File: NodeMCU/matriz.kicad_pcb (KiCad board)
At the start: 2 copper layers, 17 parts, among them J1 Conn_01x05, Q1 Q_NPN_BCE, Q2 Q_NPN_BCE, Q3 Q_NPN_BCE, SW1 SW_Push_Open, SW2 SW_Push, U3 NodeMCU1.0(ESP-12E)

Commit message: avances master
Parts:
- added w2.1: , Wire_Pads:SolderWirePad_single_0-8mmDrill, F.Cu at (97.8, 81.3)
- added w2.2: , Wire_Pads:SolderWirePad_single_0-8mmDrill, F.Cu at (97.8, 86.4)
- moved Q2 17.3 mm to (137.2, 95.2)
- moved R3 1.91 mm to (101.6, 86.4)
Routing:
- net /CLK: track 14.3 -> 96.7 mm
- net /LD: track 74.0 -> 47.6 mm
- net Net-(Q2-Pad1): track 57.8 -> 44.7 mm
- net /V+: track 252.7 -> 260.8 mm
- net Net-(R1-Pad2): track 27.7 -> 31.0 mm
- net Net-(R3-Pad2): track 6.07 -> 7.98 mm

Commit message: Cosas del dia 30 en barcara
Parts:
- removed w2.1, w2.2: , Wire_Pads:SolderWirePad_single_0-8mmDrill
- Q1, Q2, Q3: value Q_NPN_BCE -> Q_NPN_CBE
- U3: footprint NodeMCU:NodeMCU1.0(12-E) -> ESP8266:NodeMCU1.0(12-E)
- moved R2 69.8 mm to (188.0, 120.0), turned to 90 degrees
- moved R6 65.1 mm to (188.0, 96.5), turned to 270 degrees
- moved R4 52.5 mm to (172.1, 108.6)
- moved J1 49.5 mm to (189.9, 70.5)
- moved JP3 46.0 mm to (125.7, 71.8)
- moved JP4 44.9 mm to (135.3, 71.8)
- moved JP2 44.3 mm to (116.2, 71.8)
- moved SW2 44.3 mm to (144.8, 71.8)
- moved JP1 43.7 mm to (106.0, 71.8)
- moved R3 42.6 mm to (141.6, 101.0)
- moved SW1 42.3 mm to (94.6, 71.8)
- moved Q3 34.1 mm to (176.5, 86.4), turned to 90 degrees
- moved R1 31.8 mm to (127.6, 102.9)
- moved R5 31.0 mm to (156.2, 90.2)
- moved U3 29.9 mm to (106.0, 108.0)
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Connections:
- Q1 pad 1: Net-(Q1-Pad1) -> /CLK
- Q1 pad 2: /V+ -> Net-(Q1-Pad2)
- Q1 pad 3: /CLK -> GNDPWR
- Q2 pad 1: Net-(Q2-Pad1) -> /LD
- Q2 pad 2: /V+ -> Net-(Q2-Pad2)
- Q2 pad 3: /LD -> GNDPWR
- Q3 pad 1: Net-(Q3-Pad1) -> /DOUT
- Q3 pad 2: /V+ -> Net-(Q3-Pad2)
- Q3 pad 3: /DOUT -> GNDPWR
- R1 pad 1: Net-(Q1-Pad1) -> Net-(Q1-Pad2)
- R2 pad 1: GNDPWR -> /CLK
- R2 pad 2: /CLK -> /V+
- R3 pad 1: Net-(Q2-Pad1) -> Net-(Q2-Pad2)
- R4 pad 1: GNDPWR -> /LD
- R4 pad 2: /LD -> /V+
- R5 pad 1: Net-(Q3-Pad1) -> Net-(Q3-Pad2)
- R6 pad 1: GNDPWR -> /DOUT
- R6 pad 2: /DOUT -> /V+
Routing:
- net GNDPWR: track 154.6 -> 334.0 mm
- net /LD: track 47.6 -> 93.6 mm
- net Net-(Q2-Pad1): track 44.7 -> 0.00 mm
- net /V+: track 260.8 -> 220.0 mm
- net /CLK: track 96.7 -> 131.8 mm
- net Net-(R1-Pad2): track 31.0 -> 7.62 mm
- net Net-(Q3-Pad2): track 0.00 -> 19.9 mm
- net Net-(Q3-Pad1): track 15.7 -> 0.00 mm
- net /DOUT: track 57.3 -> 42.7 mm
- net Net-(R3-Pad2): track 7.98 -> 21.9 mm
- net Net-(Q2-Pad2): track 0.00 -> 11.6 mm
- net Net-(SW2-Pad2): track 42.0 -> 53.0 mm
- net Net-(Q1-Pad2): track 0.00 -> 10.4 mm
- net Net-(Q1-Pad1): track 10.3 -> 0.00 mm
- net Net-(JP2-Pad1): track 56.6 -> 48.0 mm
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
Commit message: Pistas todas de 1mm, limite y unidades mecanicas
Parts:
- added REF**: 1pin, Connectors:1pin, F.Cu at (153.0, 131.0)
- added REF**: 1pin, Connectors:1pin, F.Cu at (153.0, 68.0)
- added REF**: 1pin, Connectors:1pin, F.Cu at (88.0, 131.0)
- added REF**: 1pin, Connectors:1pin, F.Cu at (89.0, 68.0)
- J1: footprint Pin_Headers:Pin_Header_Angled_1x05_Pitch2.54mm -> Pin_Headers:Pin_Header_Straight_1x05_Pitch2.54mm
- moved R2 51.2 mm to (137.0, 115.0), turned to 0 degrees
- moved J1 47.1 mm to (143.0, 75.0)
- moved R6 44.5 mm to (145.0, 85.0)
- moved Q3 42.7 mm to (134.0, 83.0)
- moved R4 35.1 mm to (137.0, 109.0)
- moved Q2 16.0 mm to (139.0, 101.0)
- moved R5 15.5 mm to (141.0, 93.0)
- moved R3 11.8 mm to (130.0, 103.0)
- moved SW2 9.78 mm to (135.0, 72.0)
- moved JP4 8.26 mm to (127.0, 72.0)
- moved JP3 6.73 mm to (119.0, 72.0)
- moved JP2 5.21 mm to (111.0, 72.0)
- moved Q1 4.36 mm to (129.0, 112.0)
- moved JP1 4.00 mm to (102.0, 71.8)
- moved R1 3.64 mm to (124.0, 103.0)
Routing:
- net GNDPWR: track 334.0 -> 263.4 mm
- net /V+: track 220.0 -> 164.5 mm
- net /CLK: track 131.8 -> 83.0 mm
- net /LD: track 93.6 -> 72.7 mm
- net Net-(R5-Pad2): track 28.6 -> 15.0 mm
- net Net-(SW2-Pad2): track 53.0 -> 40.4 mm
- net /DOUT: track 42.7 -> 30.5 mm
- net Net-(JP4-Pad1): track 53.1 -> 41.3 mm
- net Net-(R3-Pad2): track 21.9 -> 11.1 mm
- net Net-(JP3-Pad1): track 50.6 -> 43.6 mm
- net Net-(JP1-Pad2): track 35.5 -> 30.2 mm
- net Net-(Q3-Pad2): track 19.9 -> 15.5 mm
- net Net-(R1-Pad2): track 7.62 -> 4.04 mm
- net Net-(Q2-Pad2): track 11.6 -> 8.41 mm
- net Net-(JP2-Pad1): track 48.0 -> 46.2 mm
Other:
- board outline added: 75 x 73 mm
- net class Default: trace_width 0.6 -> 1

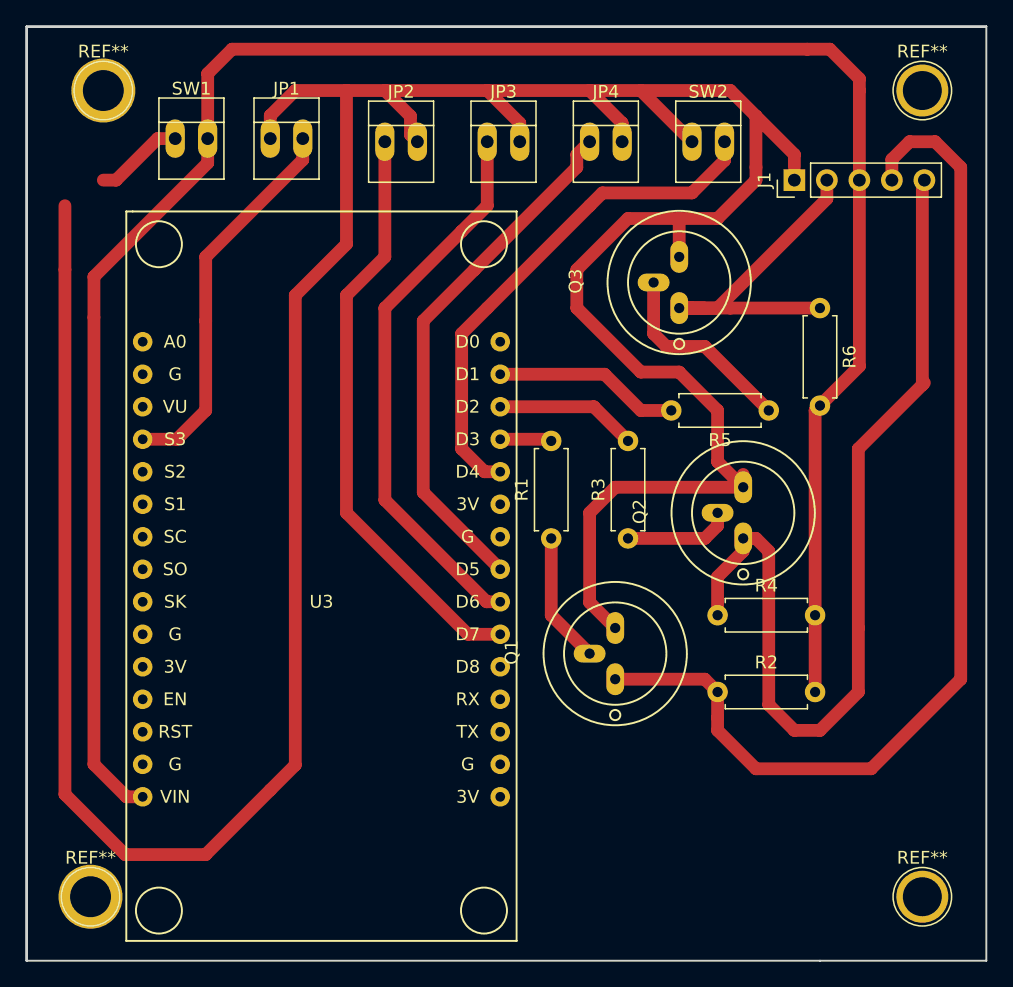
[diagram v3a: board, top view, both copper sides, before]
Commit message: Saco un jumprs y reacomodo
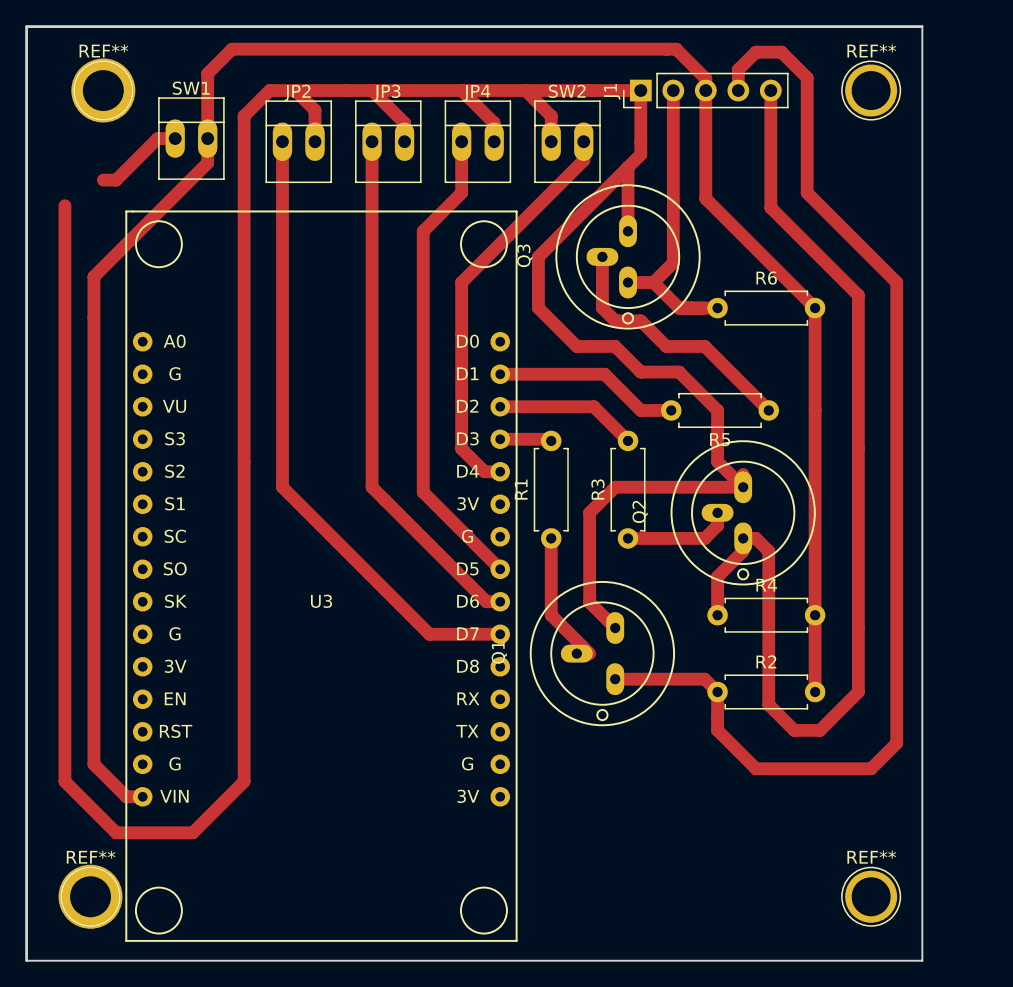
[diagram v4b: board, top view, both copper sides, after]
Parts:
- removed JP1: Jp_open_small, Connectors:PINHEAD1-2
- moved J1 13.9 mm to (131.0, 68.0)
- moved SW2 11.0 mm to (124.0, 72.0)
- moved JP4 10.0 mm to (117.0, 72.0)
- moved JP3 9.00 mm to (110.0, 72.0)
- moved JP2 8.00 mm to (103.0, 72.0)
- moved R6 8.00 mm to (137.0, 85.0), turned to 0 degrees
- moved Q3 4.47 mm to (130.0, 81.0)
- moved REF** 4.00 mm to (149.0, 131.0)
- moved REF** 4.00 mm to (149.0, 68.0)
- moved Q1 1.00 mm to (128.0, 112.0)
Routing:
- net Net-(U3-Pad4): track 30.2 -> 0.00 mm
- net GNDPWR: track 263.4 -> 238.8 mm
- net /V+: track 164.5 -> 154.6 mm
- net Net-(SW2-Pad2): track 40.4 -> 31.7 mm
- net /CLK: track 83.0 -> 90.8 mm
- net /LD: track 72.7 -> 80.1 mm
- net Net-(Q3-Pad2): track 15.5 -> 20.3 mm
- net Net-(JP4-Pad1): track 41.3 -> 37.1 mm
- net /DOUT: track 30.5 -> 26.5 mm
- net Net-(JP3-Pad1): track 43.6 -> 40.7 mm
- net Net-(JP2-Pad1): track 46.2 -> 48.8 mm
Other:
- board size 75 x 73 mm -> 70 x 73 mm

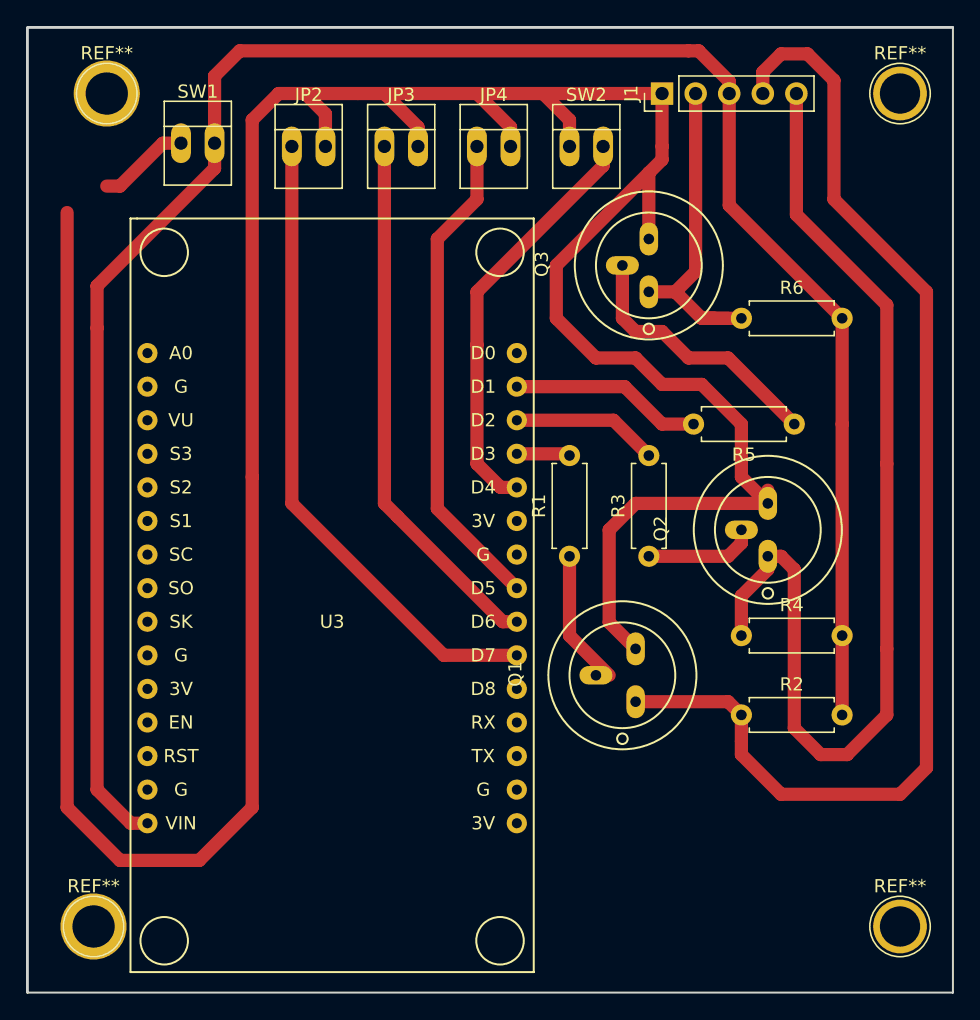
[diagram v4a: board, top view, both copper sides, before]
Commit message: Pongo las pistas en para que sea lo de atras (en verde) y minimiso espacio
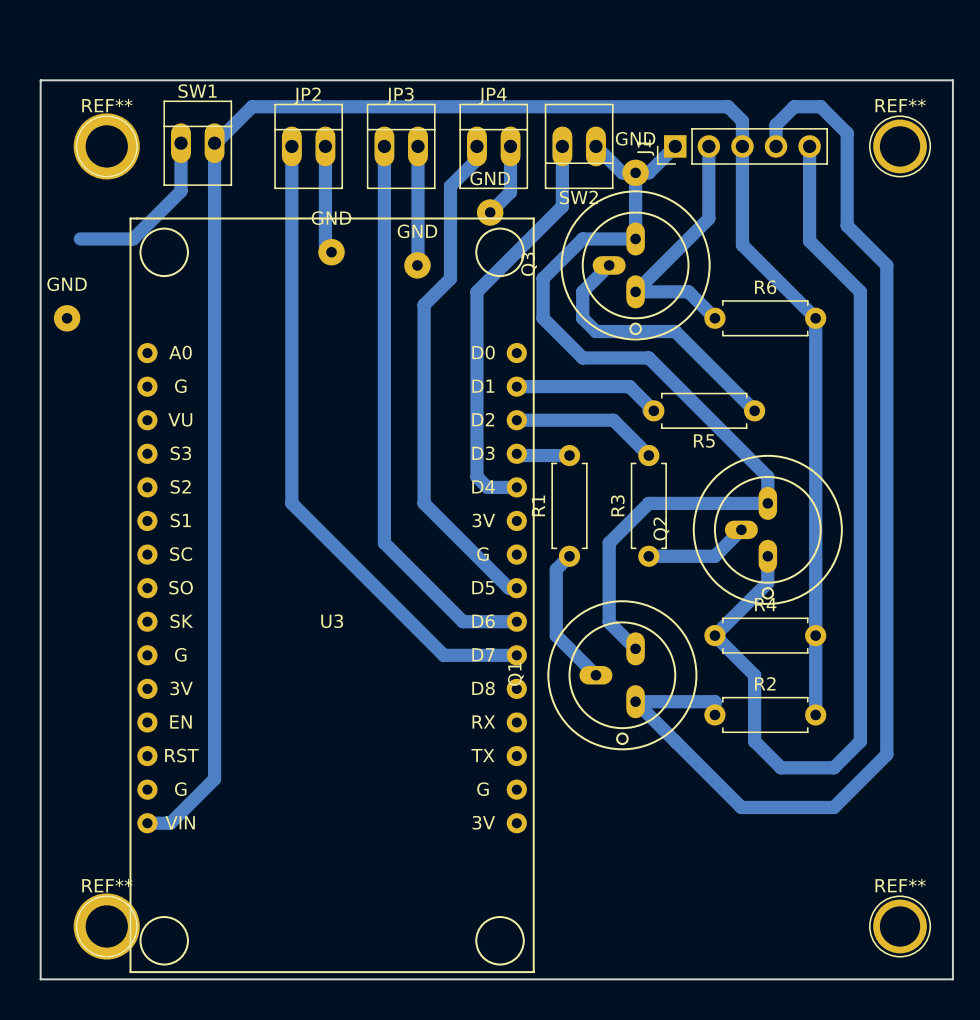
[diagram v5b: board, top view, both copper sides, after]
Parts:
- added GND: , Wire_Pads:SolderWirePad_single_0-8mmDrill, F.Cu at (106.0, 80.0)
- added GND: , Wire_Pads:SolderWirePad_single_0-8mmDrill, F.Cu at (118.0, 77.0)
- added GND: , Wire_Pads:SolderWirePad_single_0-8mmDrill, F.Cu at (129.0, 74.0)
- added GND: , Wire_Pads:SolderWirePad_single_0-8mmDrill, F.Cu at (112.5, 81.0)
- added GND: , Wire_Pads:SolderWirePad_single_0-8mmDrill, F.Cu at (86.0, 85.0)
- moved J1 4.12 mm to (132.0, 72.0)
- moved REF** 4.00 mm to (149.0, 72.0)
- moved REF** 4.00 mm to (89.0, 72.0)
- moved R5 3.16 mm to (138.0, 92.0)
- moved R2 2.00 mm to (135.0, 115.0)
- moved R4 2.00 mm to (135.0, 109.0)
- moved R6 2.00 mm to (135.0, 85.0)
- moved SW2 2.00 mm to (126.0, 72.0), turned to 180 degrees
- moved Q3 1.00 mm to (129.0, 81.0)
- moved REF** 1.00 mm to (89.0, 131.0)
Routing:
- net GNDPWR: track 238.8 -> 92.8 mm
- net /V+: track 154.6 -> 143.3 mm
- net /LD: track 80.1 -> 73.1 mm
- net /DOUT: track 26.5 -> 20.1 mm
- net +5V: track 6.96 -> 12.7 mm
- net Net-(R5-Pad2): track 15.0 -> 11.5 mm
- net /CLK: track 90.8 -> 87.6 mm
- net Net-(JP3-Pad1): track 40.7 -> 42.5 mm
- net Net-(JP4-Pad1): track 37.1 -> 38.3 mm
- net Net-(SW2-Pad2): track 31.7 -> 31.0 mm
- net Net-(Q2-Pad2): track 8.41 -> 7.83 mm
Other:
- board size 70 x 73 mm -> 69 x 68 mm

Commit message: Avances entre todos
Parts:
- R1, R3, R5: value 50KOhm -> 500Ohm
- R2, R6: value 0.7KOhm -> 1000KOhm
- R4: value 0.7KOhm -> 1000Ohm
- moved GND 0.50 mm to (129.0, 74.5)
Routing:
- net GNDPWR: track 92.8 -> 93.5 mm
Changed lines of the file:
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@@
     (links 32)
     (no_connects 3)
-    (area 82.924999 62.924999 165.85 143.700001)
+    (area 83.924999 66.88 164.85 141.700001)
     (thickness 1.6)
     (drawings 6)
-    (tracks 99)
+    (tracks 98)
     (zones 0)
     (modules 25)
@@
     (mod_text_size 1 1)
     (mod_text_width 0.15)
-    (pad_size 1.99898 1.99898)
-    (pad_drill 0.8001)
+    (pad_size 4.5 4.5)
+    (pad_drill 4)
     (pad_to_mask_clearance 0.2)
     (aux_axis_origin 0 0)
     (visible_elements 7FFFFFFF)
     (pcbplotparams
-      (layerselection 0x00030_80000001)
+      (layerselection 0x00000_80000000)
       (usegerberextensions false)
       (excludeedgelayer true)
-      (linewidth 0.100000)
+      (linewidth 1.000000)
       (plotframeref false)
       (viasonmask false)
@@
       (padsonsilk false)
       (subtractmaskfromsilk false)
-      (outputformat 1)
+      (outputformat 4)
       (mirror false)
-      (drillshape 1)
+      (drillshape 0)
       (scaleselection 1)
-      (outputdirectory ""))
+      (outputdirectory C:/Users/nahuel/git/conexiones/))
   )
   (net 0 "")
@@
       (effects (font (size 1 1) (thickness 0.15)))
     )
-    (fp_text value 50KOhm (at 3.81 2.31 90) (layer F.Fab)
+    (fp_text value 500Ohm (at 3.81 2.31 90) (layer F.Fab)
       (effects (font (size 1 1) (thickness 0.15)))
     )
@@
       (effects (font (size 1 1) (thickness 0.15)))
     )
-    (fp_text value 0.7KOhm (at 3.81 2.31) (layer F.Fab)
+    (fp_text value 1000KOhm (at 3.81 2.31) (layer F.Fab)
       (effects (font (size 1 1) (thickness 0.15)))
     )
@@
       (effects (font (size 1 1) (thickness 0.15)))
     )
-    (fp_text value 50KOhm (at 3.81 2.31 90) (layer F.Fab)
+    (fp_text value 500Ohm (at 3.81 2.31 90) (layer F.Fab)
       (effects (font (size 1 1) (thickness 0.15)))
     )
@@
       (effects (font (size 1 1) (thickness 0.15)))
     )
-    (fp_text value 0.7KOhm (at 3.81 2.31) (layer F.Fab)
+    (fp_text value 1000Ohm (at 3.81 2.31) (layer F.Fab)
       (effects (font (size 1 1) (thickness 0.15)))
     )
@@
       (effects (font (size 1 1) (thickness 0.15)))
     )
-    (fp_text value 50KOhm (at 3.81 2.31 180) (layer F.Fab)
+    (fp_text value 500Ohm (at 3.81 2.31 180) (layer F.Fab)
       (effects (font (size 1 1) (thickness 0.15)))
     )
@@
       (effects (font (size 1 1) (thickness 0.15)))
     )
-    (fp_text value 0.7KOhm (at 3.81 2.31) (layer F.Fab)
+    (fp_text value 1000KOhm (at 3.81 2.31) (layer F.Fab)
       (effects (font (size 1 1) (thickness 0.15)))
     )
@@
     (fp_circle (center 0 0) (end 2.6 0) (layer F.CrtYd) (width 0.05))
     (fp_circle (center 0 0) (end 0 -2.286) (layer F.SilkS) (width 0.12))
-    (pad 1 thru_hole circle (at 0 0) (size 4.064 4.064) (drill 3.048) (layers *.Cu *.Mask))
+    (pad 1 thru_hole circle (at 0 0) (size 4.5 4.5) (drill 4) (layers *.Cu *.Mask))
   )
   (module Connectors:1pin (layer F.Cu)
@@
     (fp_circle (center 0 0) (end 2.6 0) (layer F.CrtYd) (width 0.05))
     (fp_circle (center 0 0) (end 0 -2.286) (layer F.SilkS) (width 0.12))
-    (pad 1 thru_hole circle (at 0 0) (size 4.064 4.064) (drill 3.048) (layers *.Cu *.Mask))
+    (pad 1 thru_hole circle (at 0 0) (size 4.5 4.5) (drill 4) (layers *.Cu *.Mask))
   )
   (module Connectors:1pin (layer F.Cu)
@@
     (fp_circle (center 0 0) (end 2.6 0) (layer F.CrtYd) (width 0.05))
     (fp_circle (center 0 0) (end 0 -2.286) (layer F.SilkS) (width 0.12))
-    (pad 1 thru_hole circle (at 0 0) (size 5 5) (drill 3.2) (layers *.Cu *.Mask))
+    (pad 1 thru_hole circle (at 0 0) (size 4.5 4.5) (drill 4) (layers *.Cu *.Mask))
   )
   (module Connectors:1pin (layer F.Cu)
@@
     (fp_circle (center 0 0) (end 2.6 0) (layer F.CrtYd) (width 0.05))
     (fp_circle (center 0 0) (end 0 -2.286) (layer F.SilkS) (width 0.12))
-    (pad 1 thru_hole circle (at 0 0) (size 5 5) (drill 3.2) (layers *.Cu *.Mask))
+    (pad 1 thru_hole circle (at 0 0) (size 4.5 4.5) (drill 4) (layers *.Cu *.Mask))
   )
   (module Wire_Pads:SolderWirePad_single_0-8mmDrill (layer F.Cu)
@@
   )
   (module Wire_Pads:SolderWirePad_single_0-8mmDrill (layer F.Cu)
-    (at 129 74)
+    (at 129 74.5)
     (fp_text reference GND (at 0 -2.54) (layer F.SilkS)
       (effects (font (size 1 1) (thickness 0.15)))
@@
   (gr_line (start 153 67) (end 153 135) (angle 90) (layer Edge.Cuts) (width 0.15))
   (gr_line (start 84 67) (end 153 67) (angle 90) (layer Edge.Cuts) (width 0.15))
+  (segment (start 105.54 72) (end 105.54 79.54) (width 1) (layer B.Cu) (net 1))
+  (segment (start 105.54 79.54) (end 106 80) (width 1) (layer B.Cu) (net 1))
+  (segment (start 129 79) (end 124.5 79) (width 1) (layer B.Cu) (net 1))
+  (segment (start 139 96.5) (end 139 99) (width 1) (layer B.Cu) (net 1))
+  (segment (start 130.5 88) (end 139 96.5) (width 1) (layer B.Cu) (net 1))
+  (segment (start 125 88) (end 130.5 88) (width 1) (layer B.Cu) (net 1))
+  (segment (start 123 86) (end 125 88) (width 1) (layer B.Cu) (net 1))
+  (segment (start 123 80.5) (end 123 86) (width 1) (layer B.Cu) (net 1))
+  (segment (start 124.5 79) (end 123 80.5) (width 1) (layer B.Cu) (net 1))
+  (segment (start 129 74.5) (end 129 79) (width 1) (layer B.Cu) (net 1))
   (segment (start 119.54 72) (end 119.54 75.46) (width 1) (layer B.Cu) (net 1))
   (segment (start 119.54 75.46) (end 118 77) (width 1) (layer B.Cu) (net 1))
   (segment (start 139 99) (end 130 99) (width 1) (layer B.Cu) (net 1))
+  (segment (start 130 99) (end 127 102) (width 1) (layer B.Cu) (net 1))
+  (segment (start 127 102) (end 127 108) (width 1) (layer B.Cu) (net 1))
   (segment (start 127 108) (end 129 110) (width 1) (layer B.Cu) (net 1))
-  (segment (start 127 102) (end 127 108) (width 1) (layer B.Cu) (net 1))
-  (segment (start 130 99) (end 127 102) (width 1) (layer B.Cu) (net 1))
   (segment (start 112.54 72) (end 112.54 80.96) (width 1) (layer B.Cu) (net 1))
   (segment (start 112.54 80.96) (end 112.5 81) (width 1) (layer B.Cu) (net 1))
-  (segment (start 129 79) (end 125 79) (width 1) (layer B.Cu) (net 1))
-  (segment (start 139 97) (end 139 99) (width 1) (layer B.Cu) (net 1))
-  (segment (start 130 88) (end 139 97) (width 1) (layer B.Cu) (net 1))
-  (segment (start 125 88) (end 130 88) (width 1) (layer B.Cu) (net 1))
-  (segment (start 122 85) (end 125 88) (width 1) (layer B.Cu) (net 1))
-  (segment (start 122 82) (end 122 85) (width 1) (layer B.Cu) (net 1))
-  (segment (start 125 79) (end 122 82) (width 1) (layer B.Cu) (net 1))
-  (segment (start 129 74) (end 130 74) (width 1) (layer B.Cu) (net 1))
-  (segment (start 130 74) (end 132 72) (width 1) (layer B.Cu) (net 1))
-  (segment (start 129 74) (end 128 74) (width 1) (layer B.Cu) (net 1))
-  (segment (start 128 74) (end 126 72) (width 1) (layer B.Cu) (net 1))
-  (segment (start 129 79) (end 129 74) (width 1) (layer B.Cu) (net 1))
-  (segment (start 105.54 72) (end 105.54 79.54) (width 1) (layer B.Cu) (net 1))
   (segment (start 105.54 79.54) (end 106 80) (width 1) (layer B.Cu) (net 1))
+  (segment (start 129 75) (end 132 72) (width 1) (layer B.Cu) (net 1))
+  (segment (start 129 75) (end 126 72) (width 1) (layer B.Cu) (net 1))
   (segment (start 134.54 72) (end 134.54 77.46) (width 1) (layer B.Cu) (net 2))
   (segment (start 134.54 77.46) (end 129 83) (width 1) (layer B.Cu) (net 2))
